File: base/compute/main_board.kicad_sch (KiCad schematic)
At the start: 19 parts, among them J1 USB_C_Receptacle_USB2.0_16P, J2 Conn_01x20, J4 Conn_01x20, U1 MCP1700T-1202ETT, U3 LD1117S33TR_SOT223

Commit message: improved layout main board
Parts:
- removed D6: D_Schottky, Diode_SMD:D_SOD-323_HandSoldering, symbol Device:D_Schottky
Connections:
- net +1V2: now also C11.1
- net +3.3V: no longer C11.1
- net FPGA42: now also J2.6 (Pin_6); no longer J2.5 (Pin_5)
- net FPGA43: now also J2.7 (Pin_7); no longer J2.6 (Pin_6)
- net FPGA44: now also J2.5 (Pin_5); no longer J2.7 (Pin_7)
- net GPIO46: now reaches J2.2 (Pin_2)

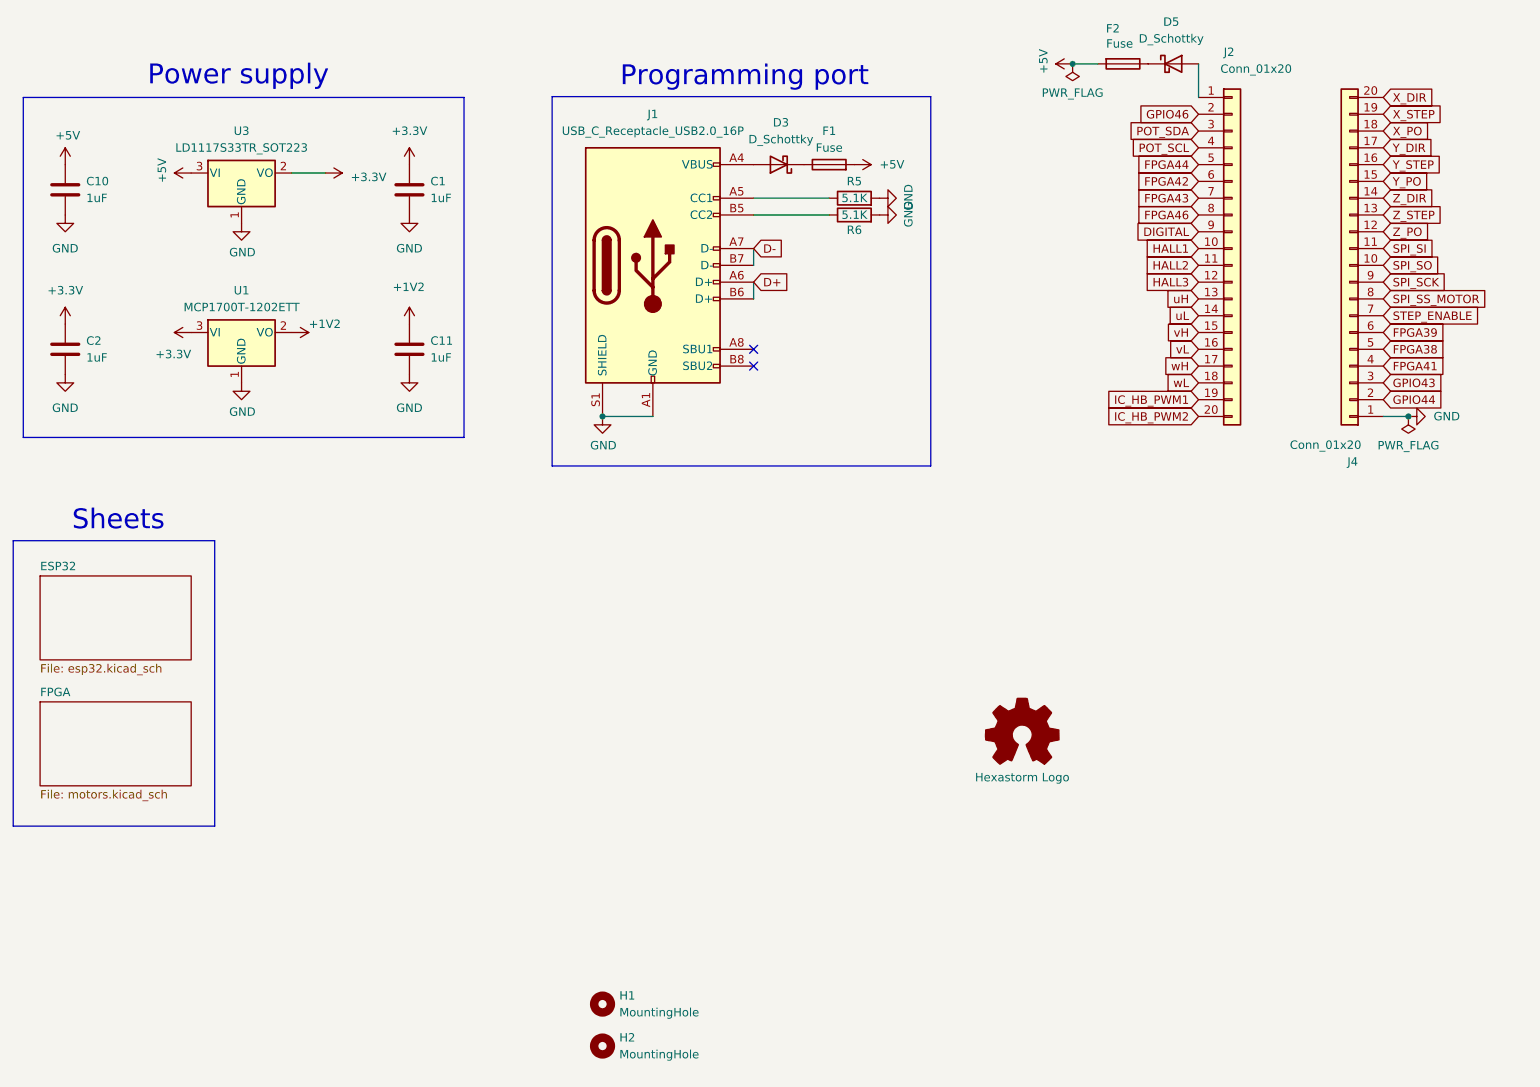
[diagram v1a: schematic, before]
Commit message: moved from 2 headers to 1 smt 40 pin header
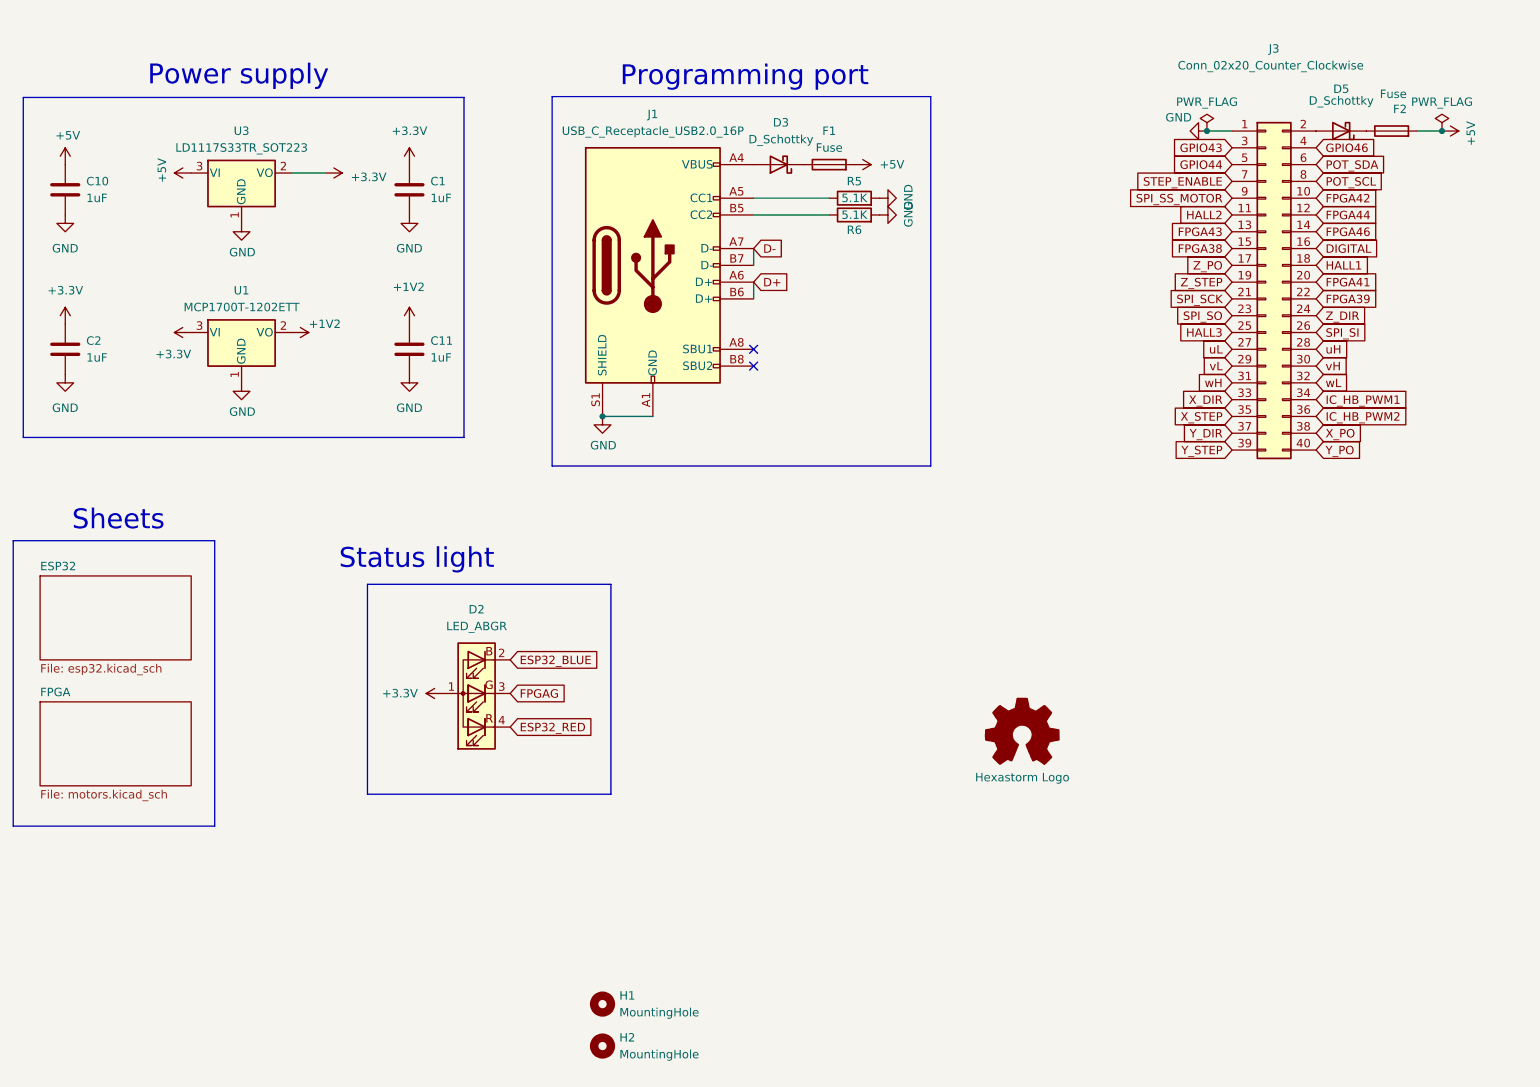
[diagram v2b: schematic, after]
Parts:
- removed J2, J4: Conn_01x20, Connector_PinHeader_2.54mm:PinHeader_1x20_P2.54mm_Vertical, symbol Connector_Generic:Conn_01x20
- added D2: LED_ABGR, footprints:LED_Cree-PLCC4_2x2mm_CW, symbol Device:LED_ABGR
- added J3: Conn_02x20_Counter_Clockwise, Connector_PinHeader_2.54mm:PinHeader_2x20_P2.54mm_Vertical_SMD, symbol Connector_Generic:Conn_02x20_Odd_Even
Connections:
- net +3.3V: now also D2.1 (A)
- net DIGITAL: now also J3.16 (Pin_16)
- net FPGA38: now also J3.15 (Pin_15)
- net FPGA39: now also J3.22 (Pin_22)
- net FPGA41: now also J3.20 (Pin_20)
- net FPGA42: now also J3.10 (Pin_10)
- net FPGA43: now also J3.13 (Pin_13)
- net FPGA44: now also J3.12 (Pin_12)
- net FPGA46: now also J3.14 (Pin_14)
- net GND: now also J3.1 (Pin_1)
- net GPIO43: now also J3.3 (Pin_3)
- net GPIO44: now also J3.5 (Pin_5)
- net GPIO46: now also J3.4 (Pin_4)
- net HALL1: now also J3.18 (Pin_18)
- net HALL2: now also J3.11 (Pin_11)
- net HALL3: now also J3.25 (Pin_25)
- net IC_HB_PWM1: now also J3.34 (Pin_34)
- net IC_HB_PWM2: now also J3.36 (Pin_36)
- net POT_SCL: now also J3.8 (Pin_8)
- net POT_SDA: now also J3.6 (Pin_6)
- net SPI_SCK: now also J3.21 (Pin_21)
- net SPI_SI: now also J3.26 (Pin_26)
- net SPI_SO: now also J3.23 (Pin_23)
- net SPI_SS_MOTOR: now also J3.9 (Pin_9)
- net STEP_ENABLE: now also J3.7 (Pin_7)
- net X_DIR: now also J3.33 (Pin_33)
- net X_PO: now also J3.38 (Pin_38)
- net X_STEP: now also J3.35 (Pin_35)
- net Y_DIR: now also J3.37 (Pin_37)
- net Y_PO: now also J3.40 (Pin_40)
- net Y_STEP: now also J3.39 (Pin_39)
- net Z_DIR: now also J3.24 (Pin_24)
- net Z_PO: now also J3.17 (Pin_17)
- net Z_STEP: now also J3.19 (Pin_19)
- net uH: now also J3.28 (Pin_28)
- net uL: now also J3.27 (Pin_27)
- net vH: now also J3.30 (Pin_30)
- net vL: now also J3.29 (Pin_29)
- net wH: now also J3.31 (Pin_31)
- net wL: now also J3.32 (Pin_32)
- net at D5.2 (A): now also J3.2 (Pin_2)
- new net ESP32_BLUE: D2.2 (BK)
- new net ESP32_RED: D2.4 (RK)
- new net FPGAG: D2.3 (GK)
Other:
- note added: "Status light"
- moved on the sheet: D5, F2

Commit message: retracking board
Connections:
- net FPGA38 is gone; now on net Z_DIR: J3.15 (Pin_15)
- net FPGA39 is gone; now on net X_STEP: J3.22 (Pin_22)
- net FPGA46 is gone; now on net Z_STEP: J3.14 (Pin_14)
- net DIGITAL: now also J3.29 (Pin_29); no longer J3.16 (Pin_16)
- net HALL1: now also J3.30 (Pin_30); no longer J3.18 (Pin_18)
- net HALL2: now also J3.31 (Pin_31); no longer J3.11 (Pin_11)
- net HALL3: now also J3.32 (Pin_32); no longer J3.25 (Pin_25)
- net IC_HB_PWM1: now also J3.39 (Pin_39); no longer J3.34 (Pin_34)
- net IC_HB_PWM2: now also J3.40 (Pin_40); no longer J3.36 (Pin_36)
- net X_DIR: now also J3.24 (Pin_24); no longer J3.33 (Pin_33)
- net X_PO: now also J3.25 (Pin_25); no longer J3.38 (Pin_38)
- net X_STEP: no longer J3.35 (Pin_35)
- net Y_DIR: now also J3.16 (Pin_16); no longer J3.37 (Pin_37)
- net Y_PO: now also J3.19 (Pin_19); no longer J3.40 (Pin_40)
- net Y_STEP: now also J3.18 (Pin_18); no longer J3.39 (Pin_39)
- net Z_DIR: no longer J3.24 (Pin_24)
- net Z_STEP: no longer J3.19 (Pin_19)
- net uH: now also J3.33 (Pin_33); no longer J3.28 (Pin_28)
- net uL: now also J3.34 (Pin_34); no longer J3.27 (Pin_27)
- net vH: now also J3.35 (Pin_35); no longer J3.30 (Pin_30)
- net vL: now also J3.36 (Pin_36); no longer J3.29 (Pin_29)
- net wH: now also J3.37 (Pin_37); no longer J3.31 (Pin_31)
- net wL: now also J3.38 (Pin_38); no longer J3.32 (Pin_32)
- net FPGA41 renamed INDEX_X
- net GPIO43 renamed UART
- net GPIO44 renamed UARX
- new net FPGA3: J3.27 (Pin_27)
- new net FPGA49: J3.28 (Pin_28)
- new net HALL2_old: J3.11 (Pin_11)

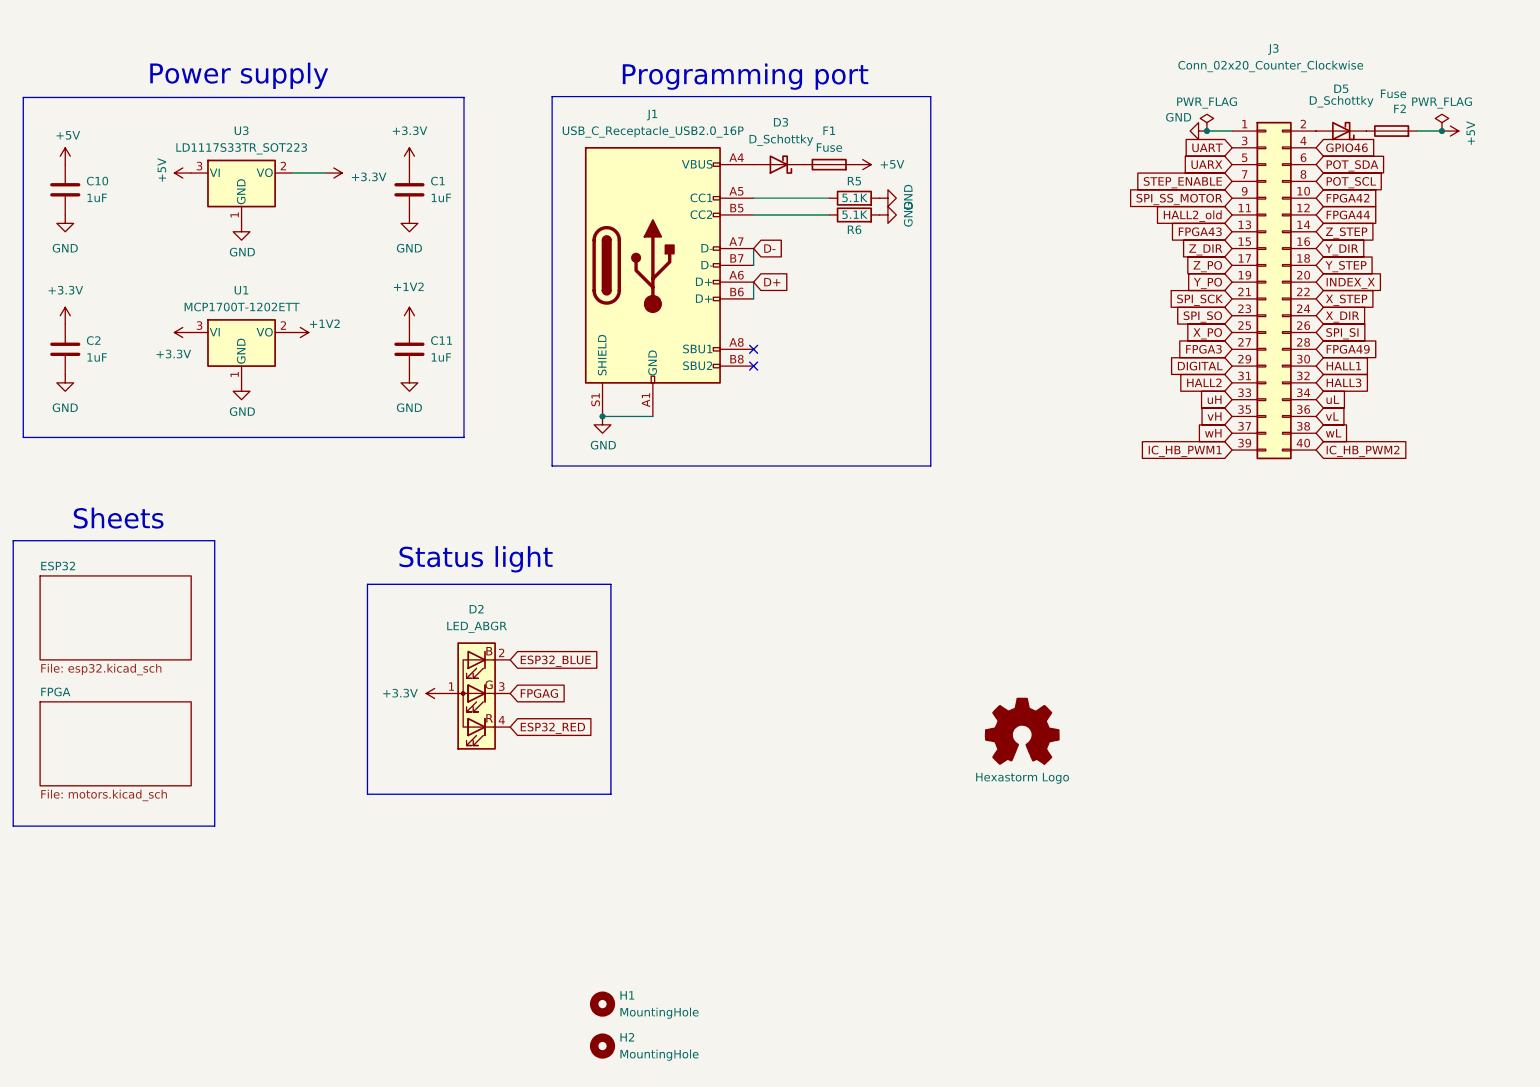
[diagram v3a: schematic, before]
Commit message: kicost integration for compute and extension
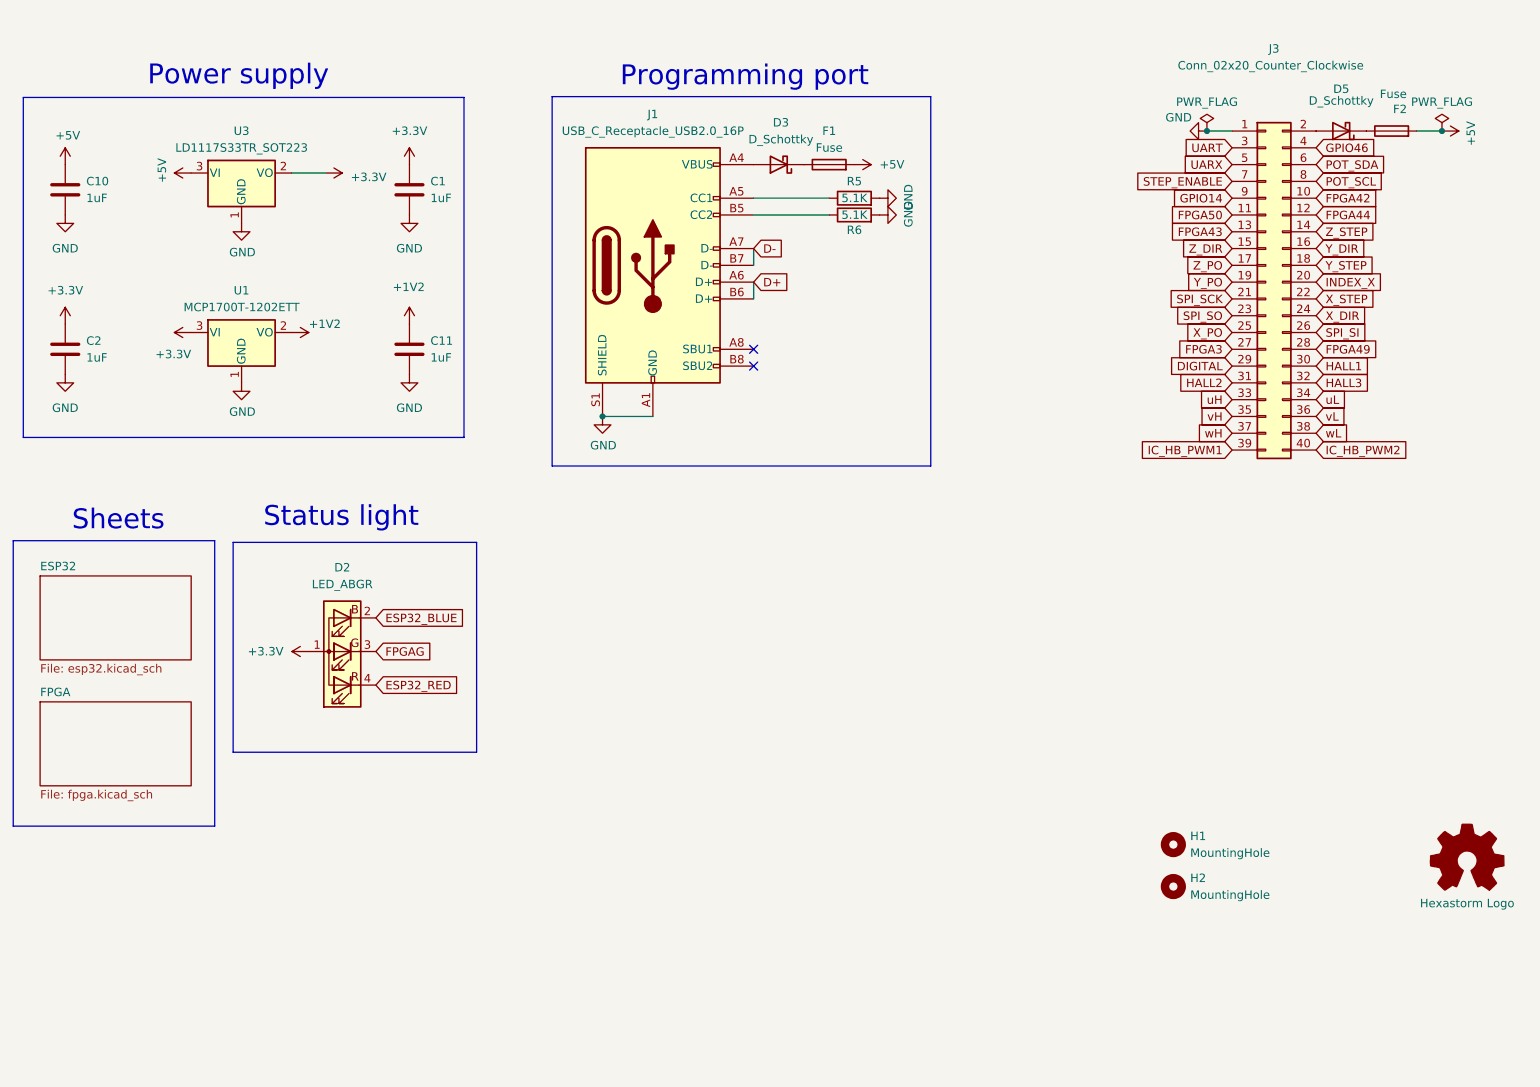
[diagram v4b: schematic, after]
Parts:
- C1, C10, C11, C2: Farnell 2094043 -> (none); Mouser 581-08055C105KAT2A -> (none); Producer 08055C105KAT2A -> (none); farnell# (none) -> 2094043; manf# (none) -> 08055C105KAT2A; mouser# (none) -> 581-08055C105KAT2A
- D2: Farnell 3625420 -> (none); Mouser 941-CLMVCFKACL1D1L71 -> (none); Producer CLMVC-FKA-CL1D1L71BB7C3C3 -> (none); farnell# (none) -> 3625420; manf# (none) -> CLMVC-FKA-CL1D1L71BB7C3C3; mouser# (none) -> 941-CLMVCFKACL1D1L71
- D3, D5: Farnell 2393466 -> (none); Mouser 78-SD103AWS-HE3-18 -> (none); Producer SD103AWS-E3-08 -> (none); farnell# (none) -> 2393466; manf# (none) -> SD103AWS-E3-08; mouser# (none) -> 78-SD103AWS-HE3-18
- F1, F2: Farnell 2799448 -> (none); Mouser 652-SF-0402FP100-2 -> (none); Producer SF-0402FP100-2 -> (none); farnell# (none) -> 2799448; manf# (none) -> SF-0402FP100-2; mouser# (none) -> 652-SF-0402FP100-2
- J1: Farnell 3588205 -> (none); Mouser 640-USB4105-GF-A -> (none); Producer USB4105-GF-A -> (none); farnell# (none) -> 3588205; manf# (none) -> USB4105-GF-A; mouser# (none) -> 640-USB4105-GF-A
- J3: Farnell TSM-120-01-L-DV -> (none); Mouser 95278-402B40LF -> (none); farnell# (none) -> TSM-120-01-L-DV; mouser# (none) -> 95278-402B40LF
- R5, R6: Farnell 1469937 -> (none); Mouser 71-CRCW0805-5.1K-E3 -> (none); Producer CRCW08055K10FKEA -> (none); farnell# (none) -> 1469937; manf# (none) -> CRCW08055K10FKEA; mouser# (none) -> 71-CRCW0805-5.1K-E3
- U1: Farnell 1851940 -> (none); Mouser 579-MCP1700T1202E/TT -> (none); Producer MCP1700T-1202E/TT -> (none); farnell# (none) -> 1851940; manf# (none) -> MCP1700T-1202E/TT; mouser# (none) -> 579-MCP1700T1202E/TT
- U3: Farnell 1467779 -> (none); Mouser 511-LD1117S33C -> (none); Producer LD1117S33CTR -> (none); farnell# (none) -> 1467779; manf# (none) -> LD1117S33CTR; mouser# (none) -> 511-LD1117S33C
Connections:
- net HALL2_old renamed FPGA50
- net SPI_SS_MOTOR renamed GPIO14
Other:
- sheet FPGA: file motors.kicad_sch -> fpga.kicad_sch
- moved on the sheet: D2, H1, H2
